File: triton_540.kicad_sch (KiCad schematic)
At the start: 46 parts, among them J1 REC ANT, J3 Conn_01x04, J4 AUX 12V, J5 KEY, J6 PTT, Q2 MPS6514, Y1 13.99MHz, Y2 14.49MHz, Y3 14.99MHz, Y4 15.49MHz

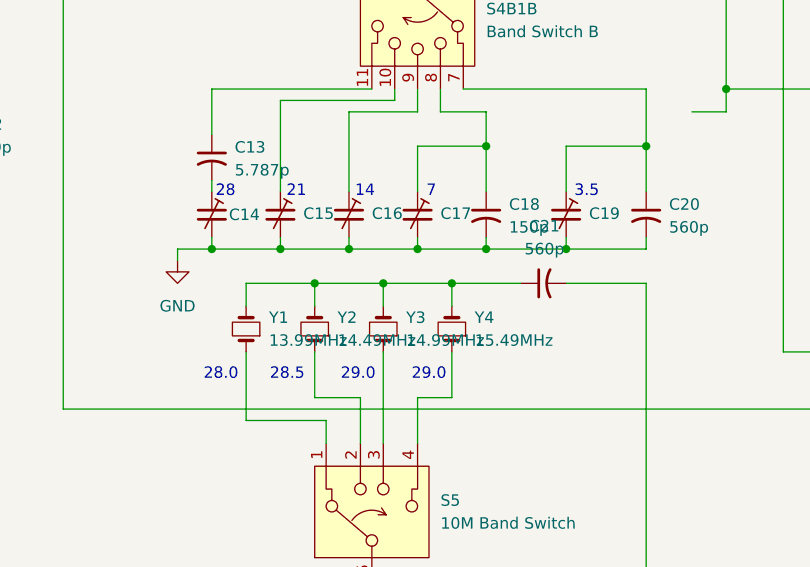
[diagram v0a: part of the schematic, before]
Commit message: Repair and re-enable 80166 simulation in the shared schematic
A fresh SPICE export contained no 80166 nets at all, and three separate faults
had accumulated during later work on the other assemblies. All three are
simulation-only; none of them affects the reconstruction of the circuit.

Sheet selection. The root schematic can only usefully simulate one assembly at
a time. RF_Amp_80166 is now included and IF-AGC_80279, VFO-80289 and
TX RX Mixer 80287 are excluded. Running a study for one of those boards means
reversing this. exclude_from_sim was also switched off on the 80166 sub-sheet's
test fixture (V7, R66-99, R66-100, C66-101, V66-1, V66-2) and on the off-board
bandswitch parts the tuned circuits need (S4, S4B1, C8-C20).

S4B1's SPICE pin map. The bandswitch is one physical rotary switch with two
wafers, drawn as two units of triton_iv:SW_Rotary_1x5_multiunit. When that
library symbol was reworked, unit 2's pins were renumbered 7-12, but S4B1's
Sim.Pins property still mapped the model's terminals to symbol pins 1-6, which
belong to unit 1. KiCad exported the switch with every terminal unconnected, so
the entire L2 tuning network -- C13 through C20 -- hung off nothing and the
output tuned circuit could not resonate. Sim.Pins now reads 7=1 8=2 ... 12=6.

A missing OUT label. The simulation-fixture area of the 80166 sub-sheet had no
local OUT label, so the provisional 1 MOhm || 5 pF output load sat on an
unnamed net instead of on the OUT pin. The load was floating.

Verified against the retained evidence after the repairs: the 29 MHz aligned
peak comes back at 28.999790 MHz against the retained 28.999365 MHz, which is
within one 0.45 kHz sweep step; Q1's source voltage and drain current reproduce
Simulation 1 exactly at 2.071 V and 4.407 mA; and the 3.500 MHz peak gain
reproduces Simulation 2 exactly at 20.189 dB. ERC reports the same 61
violations before and after, identical by type.

One naming consequence, which invalidates no evidence. The ANT and OUT pins are
w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
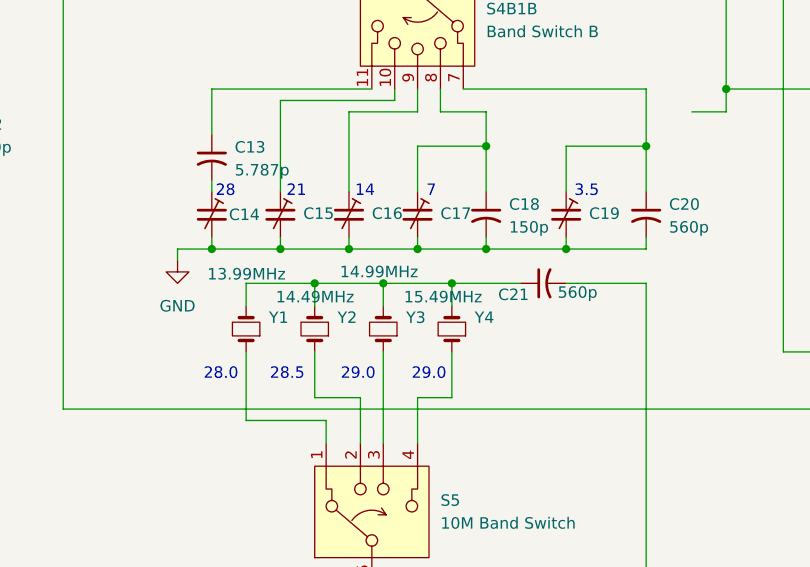
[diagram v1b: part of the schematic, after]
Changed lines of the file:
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@@
 		(unit 1)
 		(body_style 1)
-		(exclude_from_sim yes)
+		(exclude_from_sim no)
 		(in_bom yes)
 		(on_board yes)
@@
 		(unit 1)
 		(body_style 1)
-		(exclude_from_sim yes)
+		(exclude_from_sim no)
 		(in_bom yes)
 		(on_board yes)
@@
 		(in_pos_files yes)
 		(dnp no)
-		(fields_autoplaced yes)
 		(property "Reference" "Y2"
 			(at 114.3 87.6299 90)
@@
 		)
 		(property "Value" "14.49MHz"
-			(at 114.3 90.1699 90)
+			(at 107.442 85.344 90)
 			(show_name no)
 			(do_not_autoplace no)
@@
 		(unit 1)
 		(body_style 1)
-		(exclude_from_sim yes)
+		(exclude_from_sim no)
 		(in_bom yes)
 		(on_board yes)
@@
 		(unit 1)
 		(body_style 1)
-		(exclude_from_sim yes)
+		(exclude_from_sim no)
 		(in_bom yes)
 		(on_board yes)
@@
 		(unit 1)
 		(body_style 1)
-		(exclude_from_sim yes)
+		(exclude_from_sim no)
 		(in_bom yes)
 		(on_board yes)
@@
 		(unit 1)
 		(body_style 1)
-		(exclude_from_sim yes)
+		(exclude_from_sim no)
 		(in_bom yes)
 		(on_board yes)
@@
 		(unit 1)
 		(body_style 1)
-		(exclude_from_sim yes)
+		(exclude_from_sim no)
 		(in_bom yes)
 		(on_board yes)
@@
 		(unit 1)
 		(body_style 1)
-		(exclude_from_sim yes)
+		(exclude_from_sim no)
 		(in_bom yes)
 		(on_board yes)
@@
 		(unit 1)
 		(body_style 1)
-		(exclude_from_sim yes)
+		(exclude_from_sim no)
 		(in_bom yes)
 		(on_board yes)
@@
 		(unit 2)
 		(body_style 1)
-		(exclude_from_sim yes)
+		(exclude_from_sim no)
 		(in_bom yes)
 		(on_board yes)
@@
 			)
 		)
-		(property "Sim.Pins" "1=1 2=2 3=3 4=4 5=5 6=6"
+		(property "Sim.Pins" "7=1 8=2 9=3 10=4 11=5 12=6"
 			(at 123.19 54.61 0)
 			(hide yes)
@@
 		(in_pos_files yes)
 		(dnp no)
-		(fields_autoplaced yes)
 		(property "Reference" "Y4"
 			(at 129.54 87.6299 90)
@@
 		)
 		(property "Value" "15.49MHz"
-			(at 129.54 90.1699 90)
+			(at 121.666 85.344 90)
 			(show_name no)
 			(do_not_autoplace no)
@@
 		(unit 1)
 		(body_style 1)
-		(exclude_from_sim yes)
+		(exclude_from_sim no)
 		(in_bom yes)
 		(on_board yes)
@@
 		(unit 1)
 		(body_style 1)
-		(exclude_from_sim yes)
+		(exclude_from_sim no)
 		(in_bom yes)
 		(on_board yes)
@@
 		(in_pos_files yes)
 		(dnp no)
-		(fields_autoplaced yes)
 		(property "Reference" "Y3"
 			(at 121.92 87.6299 90)
@@
 		)
 		(property "Value" "14.99MHz"
-			(at 121.92 90.1699 90)
+			(at 114.554 82.55 90)
 			(show_name no)
 			(do_not_autoplace no)
@@
 		(in_pos_files yes)
 		(dnp no)
-		(fields_autoplaced yes)
 		(property "Reference" "Y1"
 			(at 106.68 87.6299 90)
@@
 		)
 		(property "Value" "13.99MHz"
-			(at 106.68 90.1699 90)
+			(at 99.822 82.804 90)
 			(show_name no)
 			(do_not_autoplace no)
@@
 		(unit 1)
 		(body_style 1)
-		(exclude_from_sim yes)
+		(exclude_from_sim no)
 		(in_bom yes)
 		(on_board yes)
@@
 		(unit 1)
 		(body_style 1)
-		(exclude_from_sim yes)
+		(exclude_from_sim no)
 		(in_bom yes)
 		(on_board yes)
@@
 		(unit 1)
 		(body_style 1)
-		(exclude_from_sim yes)
+		(exclude_from_sim no)
 		(in_bom yes)
 		(on_board yes)
@@
 		(in_pos_files yes)
 		(dnp no)
-		(fields_autoplaced yes)
 		(property "Reference" "C21"
-			(at 137.287 77.47 90)
+			(at 133.858 85.09 90)
 			(show_name no)
 			(do_not_autoplace no)
@@
 		)
 		(property "Value" "560p"
-			(at 137.287 80.01 90)
+			(at 140.97 84.836 90)
 			(show_name no)
 			(do_not_autoplace no)
@@
 		(unit 1)
 		(body_style 1)
-		(exclude_from_sim yes)
+		(exclude_from_sim no)
 		(in_bom yes)
 		(on_board yes)
@@
 		(unit 1)
 		(body_style 1)
-		(exclude_from_sim yes)
+		(exclude_from_sim no)
 		(in_bom yes)
 		(on_board yes)
@@
 		(unit 1)
 		(body_style 1)
-		(exclude_from_sim yes)
+		(exclude_from_sim no)
 		(in_bom yes)
 		(on_board yes)
@@
 		(unit 1)
 		(body_style 1)
-		(exclude_from_sim yes)
+		(exclude_from_sim no)
 		(in_bom yes)
 		(on_board yes)
@@
 		(unit 1)
 		(body_style 1)
-		(exclude_from_sim yes)
+		(exclude_from_sim no)
 		(in_bom yes)
 		(on_board yes)
@@
 		(unit 1)
 		(body_style 1)
-		(exclude_from_sim yes)
+		(exclude_from_sim no)
 		(in_bom yes)
 		(on_board yes)
@@
 		(unit 1)
 		(body_style 1)
-		(exclude_from_sim yes)
+		(exclude_from_sim no)
 		(in_bom yes)
 		(on_board yes)
@@
 		(at 38.1 15.24)
 		(size 40.64 22.86)
-		(exclude_from_sim yes)
+		(exclude_from_sim no)
 		(in_bom yes)
 		(on_board yes)
@@
 		(at 167.64 25.4)
 		(size 40.64 21.59)
-		(exclude_from_sim no)
+		(exclude_from_sim yes)
 		(in_bom yes)
 		(on_board yes)
